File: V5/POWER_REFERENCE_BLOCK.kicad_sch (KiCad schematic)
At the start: 45 parts, among them J201 3xAA_BATTERY, Q201 PMV48XP, SW201 MAIN_PWR_SW, U201 MCP3208-CI/P, U202 MCP6002-xP, U203 TPS7A2033PDBVR, U204 TPS22917DBVR, U205 TXU0304PWR, U206 TPS3899DL30DSER, U207 TPS3899DL29DSER

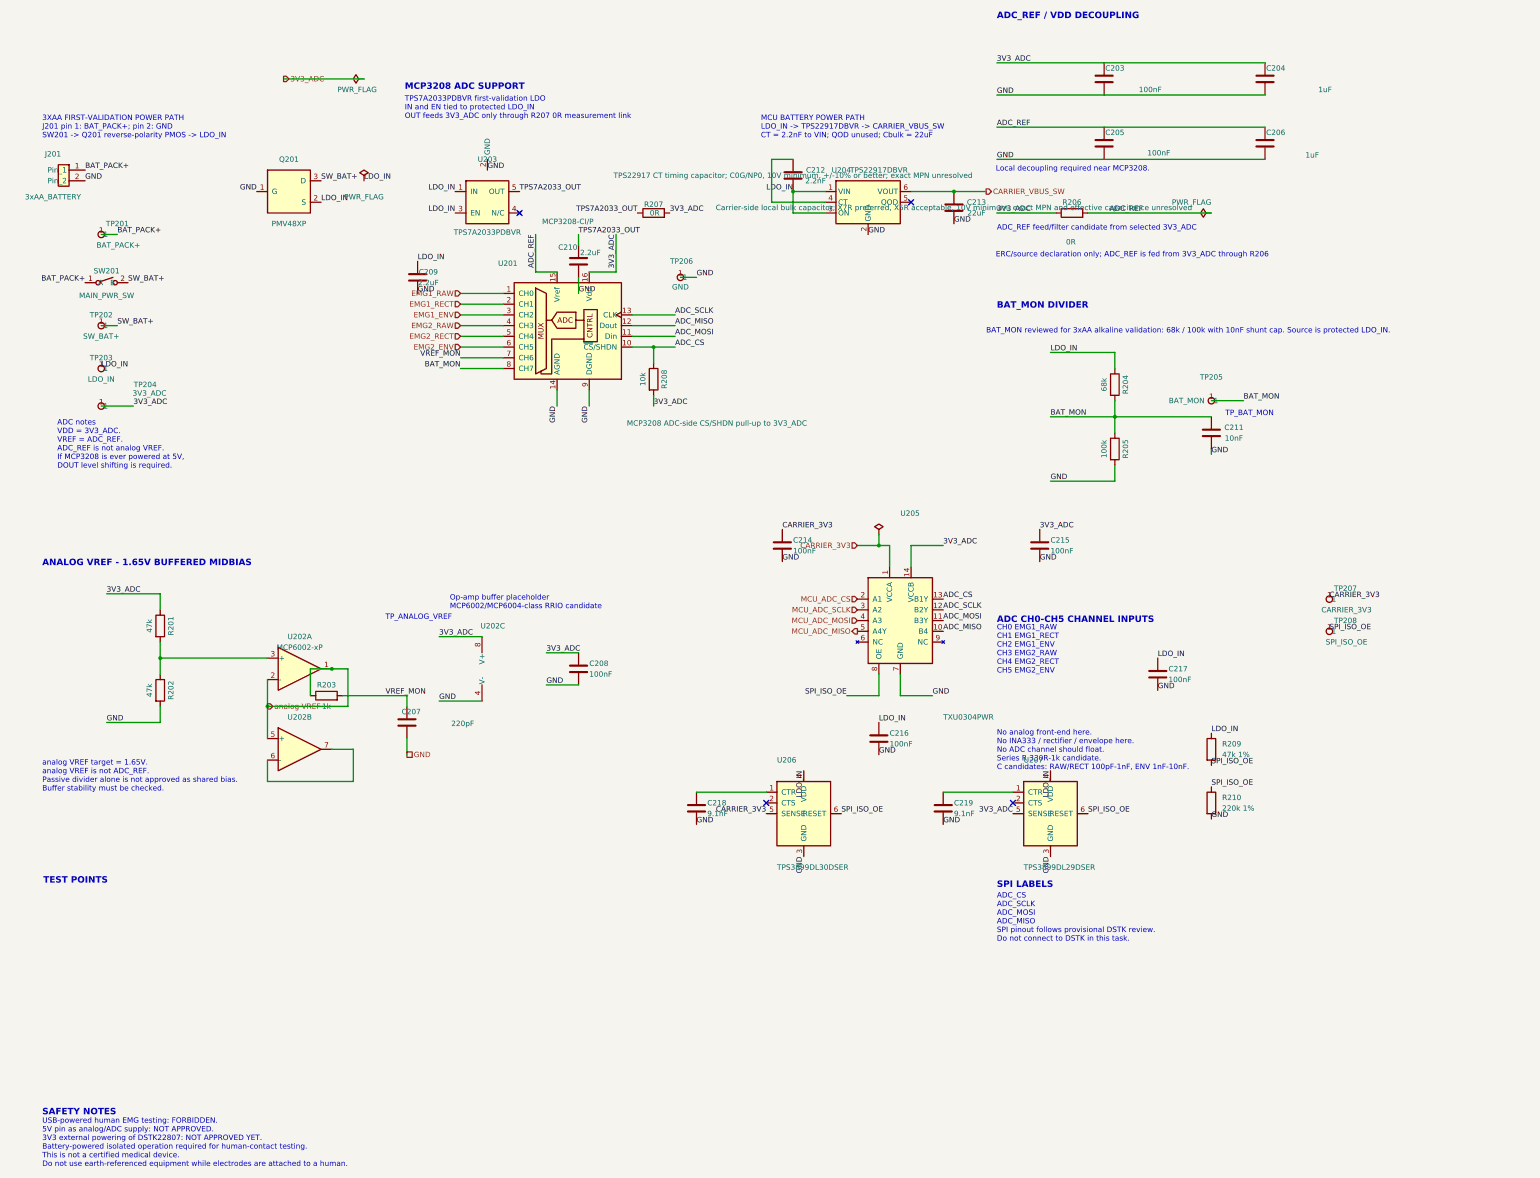
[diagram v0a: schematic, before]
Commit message: assign first passive footprint batch
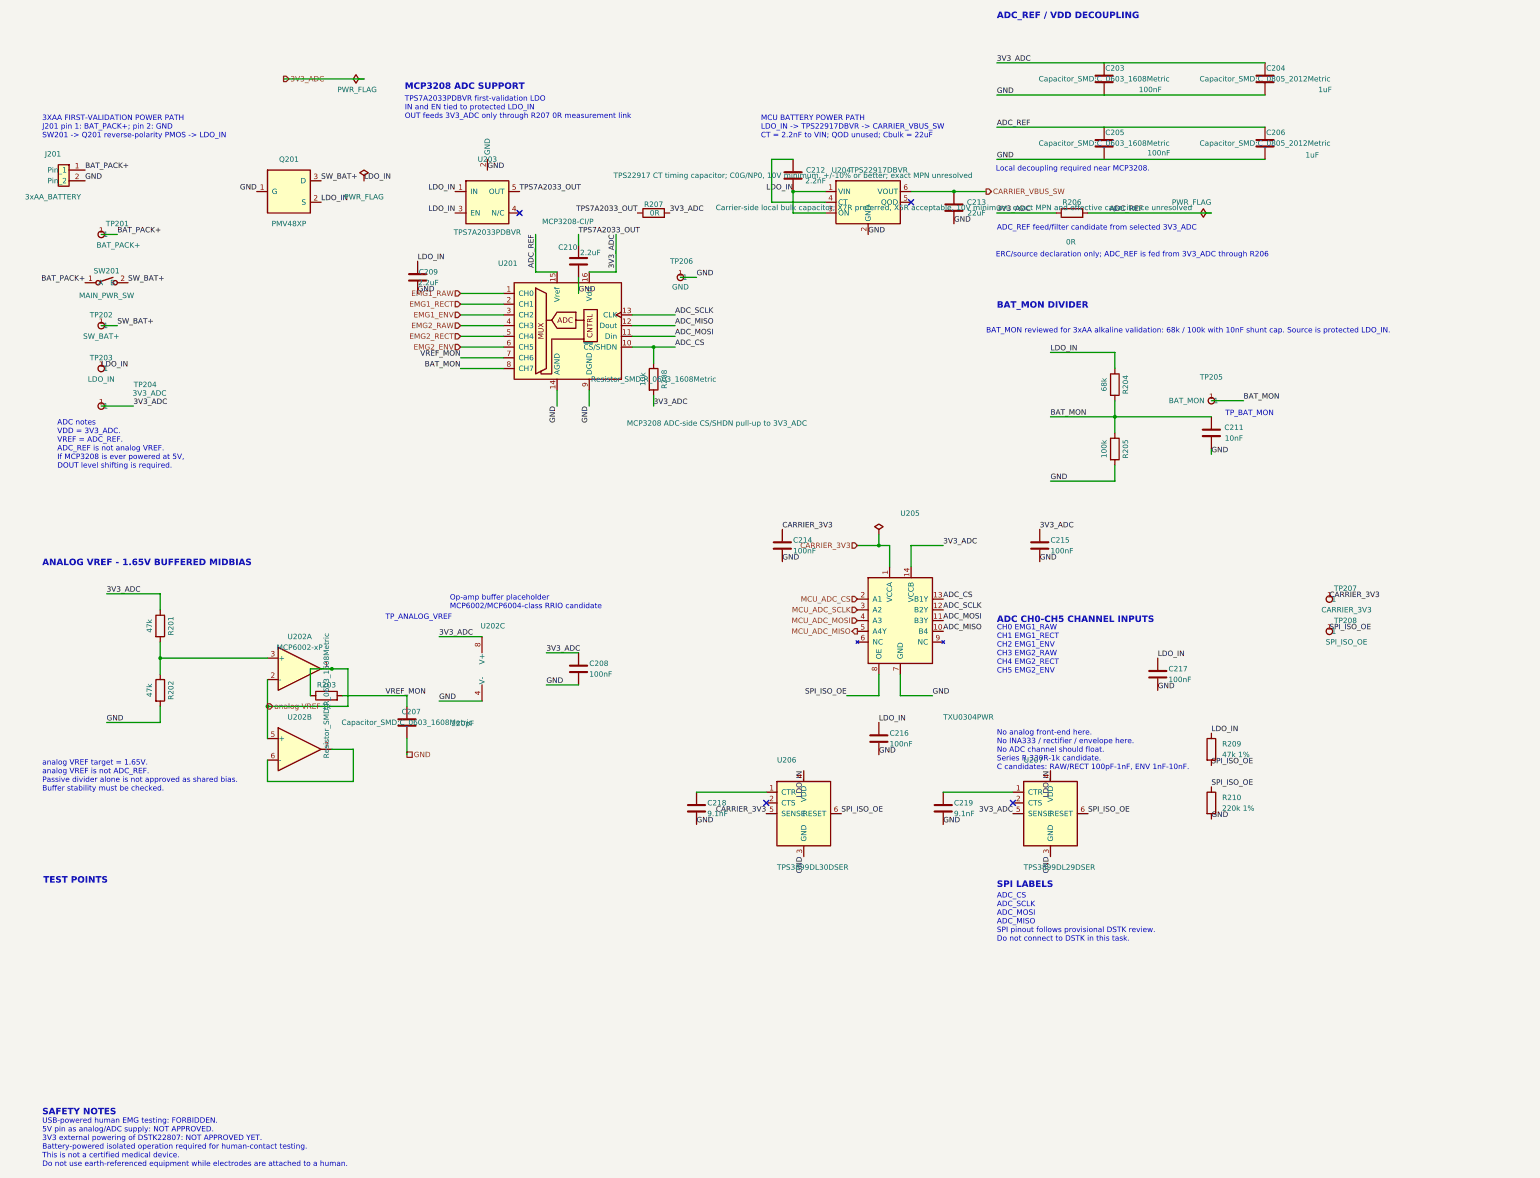
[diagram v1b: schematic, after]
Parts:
- C203, C205, C207, C208, C211, C212: footprint (none) -> Capacitor_SMD:C_0603_1608Metric
- C204, C206, C209, C210: footprint (none) -> Capacitor_SMD:C_0805_2012Metric
- R203, R206, R207, R208: footprint (none) -> Resistor_SMD:R_0603_1608Metric
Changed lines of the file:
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@@
 			)
 		)
-		(property "Footprint" ""
+		(property "Footprint" "Capacitor_SMD:C_0603_1608Metric"
 			(at 266.7 31.75 0)
 			(show_name no)
@@
 			)
 		)
-		(property "Footprint" ""
+		(property "Footprint" "Capacitor_SMD:C_0805_2012Metric"
 			(at 304.8 31.75 0)
 			(show_name no)
@@
 			)
 		)
-		(property "Footprint" ""
+		(property "Footprint" "Capacitor_SMD:C_0603_1608Metric"
 			(at 266.7 46.99 0)
 			(show_name no)
@@
 			)
 		)
-		(property "Footprint" ""
+		(property "Footprint" "Capacitor_SMD:C_0805_2012Metric"
 			(at 304.8 46.99 0)
 			(show_name no)
@@
 			)
 		)
-		(property "Footprint" ""
+		(property "Footprint" "Resistor_SMD:R_0603_1608Metric"
 			(at 82.55 177.8 0)
 			(show_name no)
@@
 			)
 		)
-		(property "Footprint" ""
+		(property "Footprint" "Capacitor_SMD:C_0603_1608Metric"
 			(at 101.6 184.15 0)
 			(show_name no)
@@
 			)
 		)
-		(property "Footprint" ""
+		(property "Footprint" "Resistor_SMD:R_0603_1608Metric"
 			(at 259.08 65.278 90)
 			(hide yes)
@@
 			)
 		)
-		(property "Footprint" ""
+		(property "Footprint" "Capacitor_SMD:C_0603_1608Metric"
 			(at 143.2052 175.26 0)
 			(hide yes)
@@
 			)
 		)
-		(property "Footprint" ""
+		(property "Footprint" "Capacitor_SMD:C_0805_2012Metric"
 			(at 105.105 82.55 0)
 			(hide yes)
@@
 			)
 		)
-		(property "Footprint" ""
+		(property "Footprint" "Capacitor_SMD:C_0805_2012Metric"
 			(at 143.205 78.74 0)
 			(hide yes)
@@
 			)
 		)
-		(property "Footprint" ""
+		(property "Footprint" "Resistor_SMD:R_0603_1608Metric"
 			(at 160.985 67.31 0)
 			(hide yes)
@@
 			)
 		)
-		(property "Footprint" ""
+		(property "Footprint" "Capacitor_SMD:C_0603_1608Metric"
 			(at 293.065 119.38 0)
 			(hide yes)
@@
 			)
 		)
-		(property "Footprint" ""
+		(property "Footprint" "Resistor_SMD:R_0603_1608Metric"
 			(at 160.02 102.87 0)
 			(show_name no)
@@
 			)
 		)
-		(property "Footprint" ""
+		(property "Footprint" "Capacitor_SMD:C_0603_1608Metric"
 			(at 194.005 58.42 0)
 			(hide yes)

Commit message: select and assign analog ic packages
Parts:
- U202: value MCP6002-xP -> MCP6002-I/SN; footprint (none) -> Package_SO:SOIC-8_3.9x4.9mm_P1.27mm
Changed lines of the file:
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@@
 			)
 		)
-		(property "Value" "MCP6002-xP"
+		(property "Value" "MCP6002-I/SN"
 			(at 76.2 166.37 0)
 			(show_name no)
@@
 			)
 		)
-		(property "Footprint" ""
+		(property "Footprint" "Package_SO:SOIC-8_3.9x4.9mm_P1.27mm"
 			(at 76.2 171.45 0)
 			(show_name no)
@@
 			)
 		)
-		(property "Value" "MCP6002-xP"
+		(property "Value" "MCP6002-I/SN"
 			(at 121.92 181.61 0)
 			(hide yes)
@@
 			)
 		)
-		(property "Footprint" ""
+		(property "Footprint" "Package_SO:SOIC-8_3.9x4.9mm_P1.27mm"
 			(at 121.92 171.45 0)
 			(hide yes)
@@
 			)
 		)
-		(property "Value" "MCP6002-xP"
+		(property "Value" "MCP6002-I/SN"
 			(at 76.2 200.66 0)
 			(hide yes)
@@
 			)
 		)
-		(property "Footprint" ""
+		(property "Footprint" "Package_SO:SOIC-8_3.9x4.9mm_P1.27mm"
 			(at 76.2 190.5 0)
 			(hide yes)

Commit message: select and assign mechanical interface parts
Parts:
- J201: value 3xAA_BATTERY -> B2B-XH-A(LF)(SN); footprint Connector_PinHeader_2.54mm:PinHeader_1x02_P2.54mm_Vertical -> Connector_JST:JST_XH_B2B-XH-A_1x02_P2.50mm_Vertical
- SW201: value MAIN_PWR_SW -> TS02CQE; footprint (none) -> EMG_V5:TS02CQE_SPST_THT
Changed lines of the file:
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@@
 			)
 		)
-		(property "Value" "3xAA_BATTERY"
+		(property "Value" "B2B-XH-A(LF)(SN)"
 			(at 17.78 59.69 0)
 			(show_name no)
@@
 			)
 		)
-		(property "Footprint" "Connector_PinHeader_2.54mm:PinHeader_1x02_P2.54mm_Vertical"
+		(property "Footprint" "Connector_JST:JST_XH_B2B-XH-A_1x02_P2.50mm_Vertical"
 			(at 20.32 62.23 0)
 			(hide yes)
@@
 			)
 		)
-		(property "Value" "MAIN_PWR_SW"
+		(property "Value" "TS02CQE"
 			(at 30.48 83.058 0)
 			(show_name no)
@@
 			)
 		)
-		(property "Footprint" ""
+		(property "Footprint" "EMG_V5:TS02CQE_SPST_THT"
 			(at 30.48 80.01 0)
 			(hide yes)
